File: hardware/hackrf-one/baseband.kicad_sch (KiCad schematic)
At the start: 136 parts

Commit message: HackRF One: update trace widths for new stack-up
correct or ignore ERC/DRC errors
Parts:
- C100, C97, C98: value (none) -> 330nF; footprint (none) -> hackrf:GSG-0402
- C101, C102, C103, C107, C108, C109, C110, C84, C85, C86, C94, C95, C96, C99: value (none) -> 22pF; footprint (none) -> hackrf:GSG-0402
- C104, C111: value (none) -> 3pF; footprint (none) -> hackrf:GSG-0402
- C105: value (none) -> 10uF; footprint (none) -> hackrf:GSG-0805
- C106: value (none) -> 1uF; footprint (none) -> hackrf:GSG-0402
- C112: value (none) -> 180pF; footprint (none) -> hackrf:GSG-0402
- C113, C119, C120, C121, C122, C123, C167, C71, C73, C75, C77, C79, C81, C83, C91: value (none) -> 100nF; footprint (none) -> hackrf:GSG-0402
- C114: value (none) -> 3.3nF; footprint (none) -> hackrf:GSG-0402
- C115: value (none) -> 33pF; footprint (none) -> hackrf:GSG-0402
- C116: value (none) -> 47pF; footprint (none) -> hackrf:GSG-0402
- C124, C72, C74, C76, C78, C80, C82: value (none) -> 2.2uF; footprint (none) -> hackrf:GSG-0402
- C159, C165, C168, C68, C69, C90: value (none) -> 100pF; footprint (none) -> hackrf:GSG-0402
- C169, C170: value (none) -> 1.8pF; footprint (none) -> hackrf:GSG-0402
- C87, C88, C89, C92, C93: value (none) -> 10nF; footprint (none) -> hackrf:GSG-0402
- D3, D9: value (none) -> GSG-DIODE-TVS-BI; footprint (none) -> hackrf:GSG-0402
- L6, L8, L9: value (none) -> DNP; footprint (none) -> hackrf:GSG-0402
- L7: value (none) -> 6.2nH; footprint (none) -> hackrf:GSG-0402
- P14: value (none) -> XCVR_CLKOUT; footprint (none) -> hackrf:GSG-TESTPOINT-50MIL
- P15: value (none) -> INTR; footprint (none) -> hackrf:GSG-TESTPOINT-50MIL
- P16: value (none) -> CLKIN; footprint (none) -> hackrf:GSG-SMA-73251-2120
- P18: value (none) -> OEB; footprint (none) -> hackrf:GSG-TESTPOINT-50MIL
- P2: value (none) -> CLKOUT; footprint (none) -> hackrf:GSG-SMA-73251-2120
- P37: value (none) -> SCL; footprint (none) -> hackrf:GSG-TESTPOINT-50MIL
- P38: value (none) -> SDA; footprint (none) -> hackrf:GSG-TESTPOINT-50MIL
- P39: value (none) -> SSP1_SCK; footprint (none) -> hackrf:GSG-TESTPOINT-50MIL
- P40: value (none) -> SSP1_COPI; footprint (none) -> hackrf:GSG-TESTPOINT-50MIL
- P41: value (none) -> SSP1_CIPO; footprint (none) -> hackrf:GSG-TESTPOINT-50MIL
- P53: value (none) -> CS_XCVR; footprint (none) -> hackrf:GSG-TESTPOINT-50MIL
- P54: value (none) -> CS_AD; footprint (none) -> hackrf:GSG-TESTPOINT-50MIL
- P55: value (none) -> TXENABLE; footprint (none) -> hackrf:GSG-TESTPOINT-50MIL
- P56: value (none) -> RXENABLE; footprint (none) -> hackrf:GSG-TESTPOINT-50MIL
- P57: value (none) -> XTAL2; footprint (none) -> hackrf:GSG-TESTPOINT-50MIL
- P58: value (none) -> GCK1; footprint (none) -> hackrf:GSG-TESTPOINT-50MIL
- P59: value (none) -> GCK2; footprint (none) -> hackrf:GSG-TESTPOINT-50MIL
- P60: value (none) -> SGPIO_CLK; footprint (none) -> hackrf:GSG-TESTPOINT-50MIL
- P61: value (none) -> DA0; footprint (none) -> hackrf:GSG-TESTPOINT-50MIL
- P62: value (none) -> DA7; footprint (none) -> hackrf:GSG-TESTPOINT-50MIL
- P63: value (none) -> DD0; footprint (none) -> hackrf:GSG-TESTPOINT-50MIL
- P64: value (none) -> DD9; footprint (none) -> hackrf:GSG-TESTPOINT-50MIL
- P65: value (none) -> DA4; footprint (none) -> hackrf:GSG-TESTPOINT-50MIL
- P66: value (none) -> DD5; footprint (none) -> hackrf:GSG-TESTPOINT-50MIL
- P67: value (none) -> RSSI; footprint (none) -> hackrf:GSG-TESTPOINT-50MIL
- P83, P84, P85, P86, P87, P88, P89, P90, P91, P92: value (none) -> GND; footprint (none) -> hackrf:GSG-TESTPOINT-50MIL
- P9: value (none) -> BASEBAND; footprint (none) -> hackrf:GSG-HEADER-2x8
- Q3: value (none) -> MOSFET_P; footprint (none) -> gsg-modules:SOT23-3
- R10, R13, R8, R9: value (none) -> 1k; footprint (none) -> hackrf:GSG-0402
- R104, R105, R11, R41, R85: value (none) -> 10k; footprint (none) -> hackrf:GSG-0402
- R14, R15, R16, R17: value (none) -> 4k7; footprint (none) -> hackrf:GSG-0402
- R20, R21, R22, R23: value (none) -> 0; footprint (none) -> hackrf:GSG-0402
- R25, R26: value (none) -> 475; footprint (none) -> hackrf:GSG-0402
- R27, R28: value (none) -> 1k8; footprint (none) -> hackrf:GSG-0402
- R31, R32, R33, R94: value (none) -> 39; footprint (none) -> hackrf:GSG-0402
- T3: value (none) -> RX_BALUN; footprint (none) -> hackrf:GSG-2500BL14M100
- T4: value (none) -> TX_BALUN; footprint (none) -> hackrf:GSG-2500BL14M100
- U17: value (none) -> MAX2837; footprint (none) -> hackrf:GSG-QFN48-6
- U18: value (none) -> MAX5864; footprint (none) -> hackrf:GSG-QFN48-7
- U19: value (none) -> SI5351C; footprint (none) -> hackrf:GSG-QFN20-4
- X1: value (none) -> GSG-XTAL4PIN; footprint (none) -> hackrf:GSG-XTAL3.2x2.5mm

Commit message: HackRF One: correct or ignore ERC errors
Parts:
- T4: symbol hackrf:BALUN -> gsg-symbols:BALUN
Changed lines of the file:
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@@
     (pin "2")
   )
-  (symbol (lib_id "hackrf:BALUN") (at 119.38 114.3 180) (unit 1)
+  (symbol (lib_name "BALUN_1") (lib_id "hackrf:BALUN") (at 119.38 114.3 180) (unit 1)
     (in_bom yes) (on_board yes)
     (property "Reference" "T3" (id 0) (at 119.38 120.65 0)
@@
     )
     (property "Datasheet" "" (id 3) (at 119.38 114.3 0)
-      (effects (font (size 1.524 1.524)) hide)
+      (effects (font (size 1.524 1.524)))
     )
     (property "Manufacturer" "Johanson Technology" (id 4) (at 119.38 114.3 0)
@@
     (pin "1")
   )
-  (symbol (lib_id "hackrf:BALUN") (at 119.38 142.24 180) (unit 1)
+  (symbol (lib_id "gsg-symbols:BALUN") (at 119.38 142.24 180) (unit 1)
     (in_bom yes) (on_board yes)
     (property "Reference" "T4" (id 0) (at 119.38 148.59 0)
@@
     )
     (property "Datasheet" "" (id 3) (at 119.38 142.24 0)
-      (effects (font (size 1.524 1.524)) hide)
+      (effects (font (size 1.524 1.524)))
     )
     (property "Manufacturer" "Johanson Technology" (id 4) (at 119.38 142.24 0)

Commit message: HackRF One: update dates
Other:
- company: Copyright 2012-2020 Great Scott Gadgets -> Copyright 2012-2022 Great Scott Gadgets
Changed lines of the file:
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@@
   (title_block
     (title "HackRF One")
-    (date "2021-09-28")
+    (date "2022-08-28")
     (rev "r9")
-    (company "Copyright 2012-2020 Great Scott Gadgets")
+    (company "Copyright 2012-2022 Great Scott Gadgets")
     (comment 1 "Michael Ossmann")
     (comment 2 "Licensed under the CERN-OHL-P v2")

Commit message: HackRF One: add diode to Q4 output
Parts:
- T3: symbol hackrf:BALUN -> gsg-symbols:BALUN
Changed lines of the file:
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@@
     (pin "2")
   )
-  (symbol (lib_name "BALUN_1") (lib_id "hackrf:BALUN") (at 119.38 114.3 180) (unit 1)
+  (symbol (lib_id "gsg-symbols:BALUN") (at 119.38 114.3 180) (unit 1)
     (in_bom yes) (on_board yes)
     (property "Reference" "T3" (id 0) (at 119.38 120.65 0)

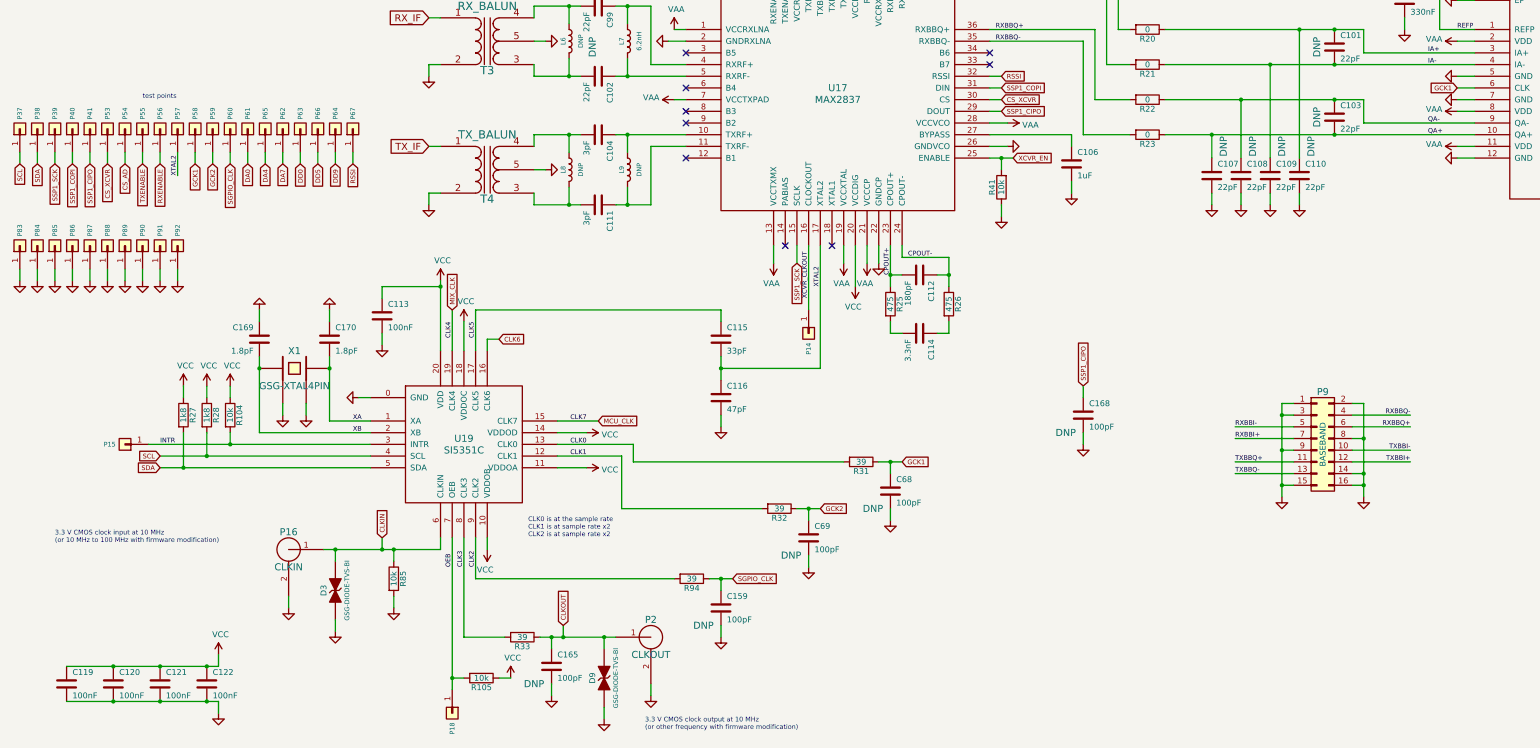
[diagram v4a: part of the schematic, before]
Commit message: HackRF One: change U19 from Si5351C to Si5351A
add clock distribution and detection
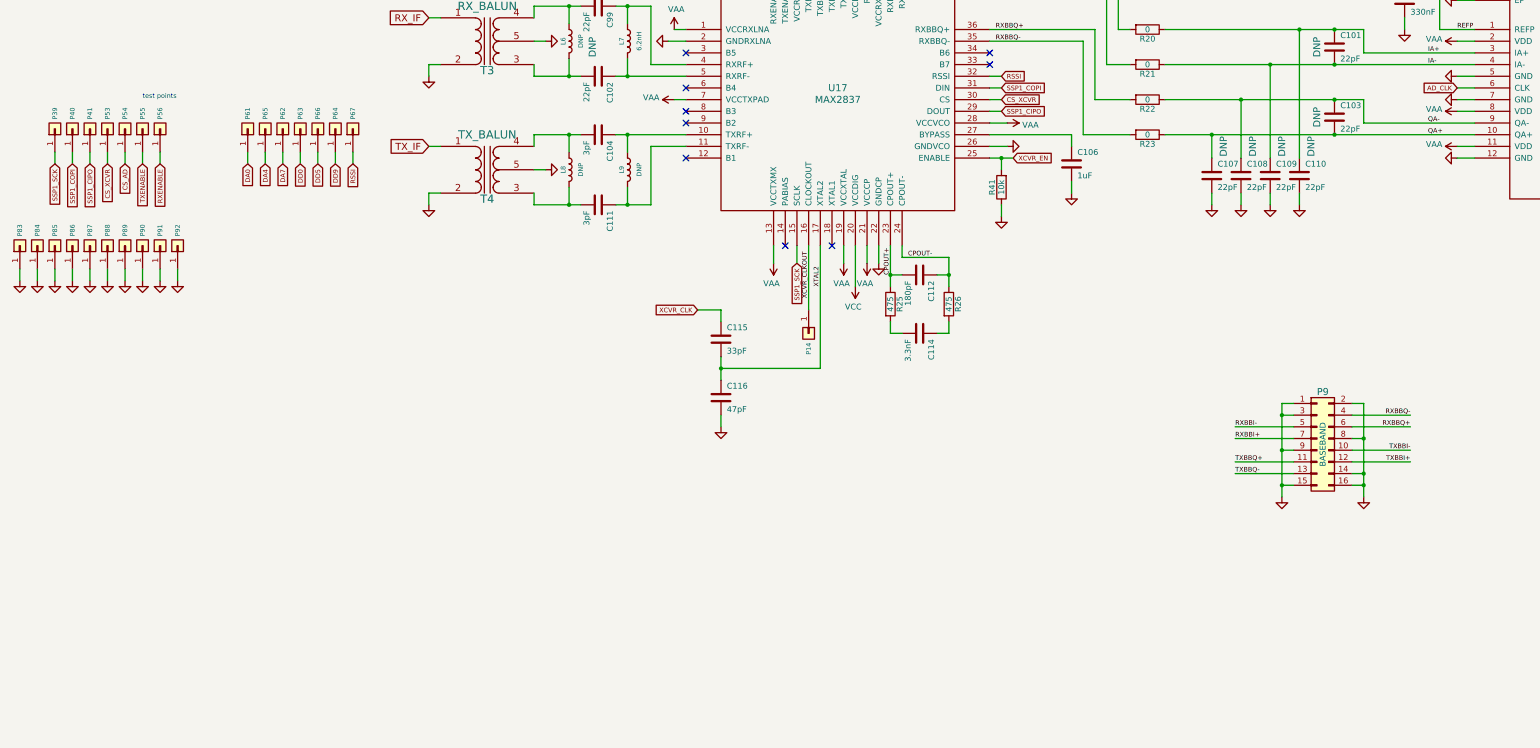
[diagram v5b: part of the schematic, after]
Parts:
- removed C113, C119, C120, C121, C122: 100nF, hackrf:GSG-0402, symbol Device:C
- removed C159, C165, C168, C68, C69: 100pF, hackrf:GSG-0402, symbol Device:C
- removed C169, C170: 1.8pF, hackrf:GSG-0402, symbol Device:C
- removed D3, D9: GSG-DIODE-TVS-BI, hackrf:GSG-0402, symbol hackrf:GSG-DIODE-TVS-BI
- removed P15: INTR, hackrf:GSG-TESTPOINT-50MIL, symbol Connector_Generic:Conn_01x01
- removed P16: CLKIN, hackrf:GSG-SMA-73251-2120, symbol hackrf:GSG-RF-CONN
- removed P18: OEB, hackrf:GSG-TESTPOINT-50MIL, symbol Connector_Generic:Conn_01x01
- removed P2: CLKOUT, hackrf:GSG-SMA-73251-2120, symbol hackrf:GSG-RF-CONN
- removed P37: SCL, hackrf:GSG-TESTPOINT-50MIL, symbol Connector_Generic:Conn_01x01
- removed P38: SDA, hackrf:GSG-TESTPOINT-50MIL, symbol Connector_Generic:Conn_01x01
- removed P57: XTAL2, hackrf:GSG-TESTPOINT-50MIL, symbol Connector_Generic:Conn_01x01
- removed P58: GCK1, hackrf:GSG-TESTPOINT-50MIL, symbol Connector_Generic:Conn_01x01
- removed P59: GCK2, hackrf:GSG-TESTPOINT-50MIL, symbol Connector_Generic:Conn_01x01
- removed P60: SGPIO_CLK, hackrf:GSG-TESTPOINT-50MIL, symbol Connector_Generic:Conn_01x01
- removed R104, R105, R85: 10k, hackrf:GSG-0402, symbol Device:R
- removed R27, R28: 1k8, hackrf:GSG-0402, symbol Device:R
- removed R31, R32, R33, R94: 39, hackrf:GSG-0402, symbol Device:R
- removed U19: SI5351C, hackrf:GSG-QFN20-4, symbol hackrf:SI5351C
- removed X1: GSG-XTAL4PIN, hackrf:GSG-XTAL3.2x2.5mm, symbol hackrf:GSG-XTAL4PIN
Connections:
- net CLK5 renamed XCVR_CLK
- net GCK1 renamed AD_CLK
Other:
- note removed: "3.3 V CMOS clock input at 10 MHz (or 10 MHz to 100 MHz with firmware modification)"
- note removed: "3.3 V CMOS clock output at 10 MHz (or other frequency with firmware modification)"
- note removed: "CLK0 is at the sample rate CLK1 is at sample rate x2 CLK2 is at sample rate x2"
